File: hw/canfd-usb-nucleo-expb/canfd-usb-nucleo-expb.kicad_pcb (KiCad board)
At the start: 2 copper layers, 70 x 59 mm, 52 parts, among them CN10 CONN, CN7 POWER, J3 Conn_01x03, J4 Conn_01x03, J5 Conn_01x03, SW1 SW_Push_Dual_x2, SW2 SW_Push_Dual_x2, SW3 SW_Push_Dual_x2, U2 ATA6561-GAQW-N, U3 ATA6561-GAQW-N, U4 ATA6561-GAQW-N

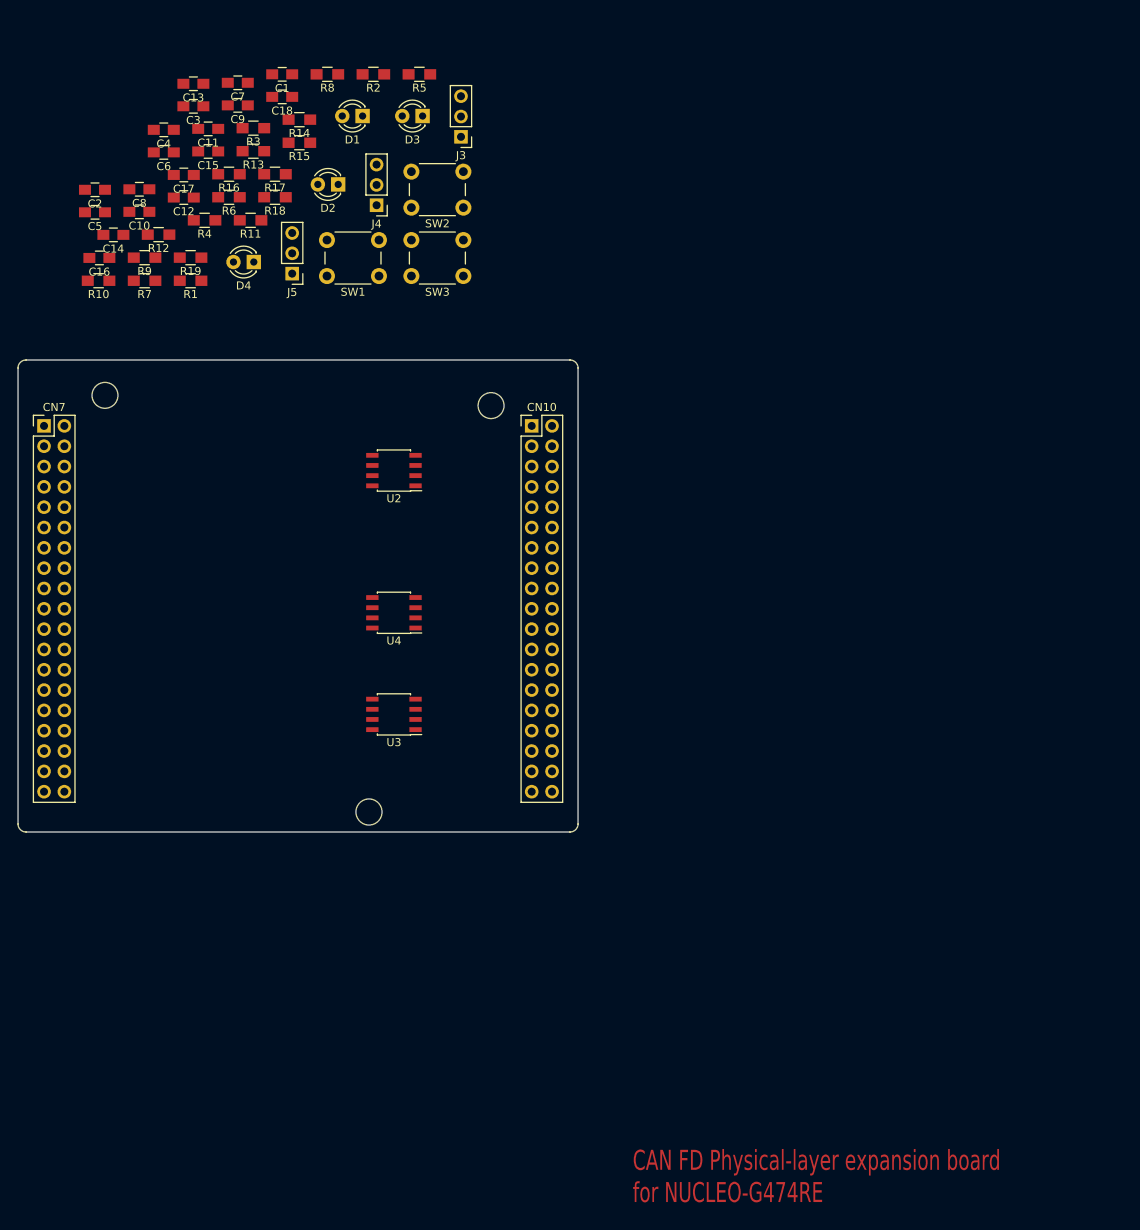
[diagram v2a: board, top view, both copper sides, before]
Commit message: HW: Added footprints for all components
Created the footprint for USB-Type-C connector
Added footprints for the rest of the components on the PCB.
Started the mock-up placement of components on the board

Signed-off-by: AlexeyZ <silkt207@gmail.com>
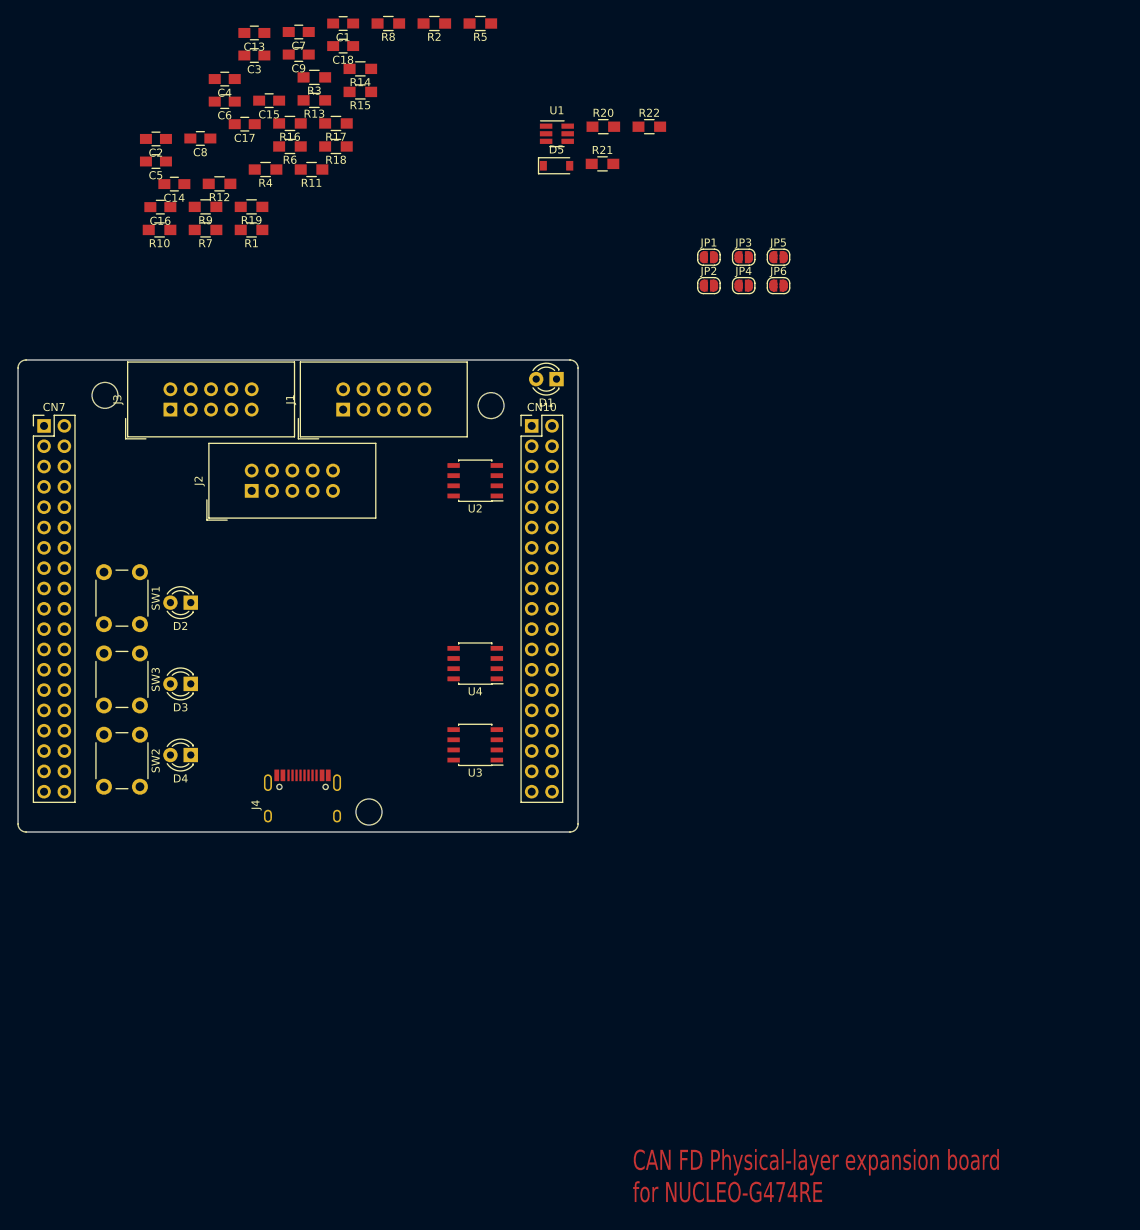
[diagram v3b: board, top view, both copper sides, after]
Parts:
- removed C10, C11, C12: 100p, Capacitors_SMD:C_0805_HandSoldering
- removed J5: Conn_01x03, Pin_Headers:Pin_Header_Straight_1x03_Pitch2.54mm
- added D5: D_Schottky, Diodes_SMD:D_SOD-123, F.Cu at (169.5, 45.6)
- added J1: Conn_01x10, can-usb:IDC-Header_2x05_P2.54mm_Vertical, F.Cu at (142.9, 76.1)
- added J2: Conn_01x10, can-usb:IDC-Header_2x05_P2.54mm_Vertical, F.Cu at (131.4, 86.2)
- added JP1: Jumper_2_Open, can-usb:SolderJumper-2_P1.3mm_Open_RoundedPad1.0x1.5mm, F.Cu at (188.6, 57.0)
- added JP2: Jumper_2_Open, can-usb:SolderJumper-2_P1.3mm_Open_RoundedPad1.0x1.5mm, F.Cu at (188.6, 60.6)
- added JP3: Jumper_2_Open, can-usb:SolderJumper-2_P1.3mm_Open_RoundedPad1.0x1.5mm, F.Cu at (192.9, 57.0)
- added JP4: Jumper_2_Open, can-usb:SolderJumper-2_P1.3mm_Open_RoundedPad1.0x1.5mm, F.Cu at (192.9, 60.6)
- added JP5: Jumper_2_Open, can-usb:SolderJumper-2_P1.3mm_Open_RoundedPad1.0x1.5mm, F.Cu at (197.3, 57.0)
- added JP6: Jumper_2_Open, can-usb:SolderJumper-2_P1.3mm_Open_RoundedPad1.0x1.5mm, F.Cu at (197.3, 60.6)
- added R20: 100R, Resistors_SMD:R_0805_HandSoldering, F.Cu at (175.4, 40.7)
- added R21: 100R, Resistors_SMD:R_0805_HandSoldering, F.Cu at (175.3, 45.4)
- added R22: 100R, Resistors_SMD:R_0805_HandSoldering, F.Cu at (181.1, 40.7)
- added U1: USBLC6-2SC6, TO_SOT_Packages_SMD:SOT-23-6_Handsoldering, F.Cu at (169.6, 41.6)
- C4: value 15p -> 10nf
- C5: value 15p -> 22u
- C6: value 15p -> 2.2u
- J3: value Conn_01x03 -> Conn_01x10; footprint Pin_Headers:Pin_Header_Straight_1x03_Pitch2.54mm -> can-usb:IDC-Header_2x05_P2.54mm_Vertical
- J4: value Conn_01x03 -> USB_C_Receptacle_USB2.0; footprint Pin_Headers:Pin_Header_Straight_1x03_Pitch2.54mm -> can-usb:L-KLS1-TIPEC-B
- R1: value 62R -> 220k
- R12: value 100k -> 5.1k
- R13, R14, R19: value 100k -> 10k
- R15, R16, R17, R18: value 100k -> 510R
- R2, R3, R4: value 62R -> 1k
- R5: value 62R -> 5.1k
- moved SW2 77.3 mm to (117.5, 116.7), turned to 270 degrees
- moved D3 76.7 mm to (123.8, 110.4)
- moved J4 71.9 mm to (137.8, 121.8), turned to 0 degrees
- moved SW3 62.1 mm to (117.5, 106.6), turned to 270 degrees
- moved D4 62.1 mm to (123.8, 119.3)
- moved D2 55.4 mm to (123.8, 100.2)
- moved J3 49.8 mm to (121.3, 76.1), turned to 90 degrees
- moved SW1 47.6 mm to (117.5, 96.4), turned to 270 degrees
- moved D1 40.9 mm to (169.5, 72.3)
- moved U4 12.0 mm to (159.4, 107.8)
- moved U3 10.9 mm to (159.4, 118.0)
- moved U2 10.2 mm to (159.4, 85.0)
- moved C13 9.92 mm to (131.8, 29.0)
- moved C16 9.92 mm to (120.0, 50.8)
- moved C8 9.92 mm to (125.0, 42.2)
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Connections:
- C16 pad 1: +3V3 -> Net-(C16-Pad1)
- C17 pad 1: +3V3 -> Net-(C17-Pad1)
- C18 pad 1: +3V3 -> Net-(C18-Pad1)
- C4 pad 1: RX1 -> Net-(C4-Pad1)
- C5 pad 1: RX2 -> +5V
- C6 pad 1: RX3 -> +3V3
- CN10 pad 22: (no net) -> Net-(CN10-Pad22)
- CN10 pad 24: (no net) -> Net-(CN10-Pad24)
- CN10 pad 26: (no net) -> Net-(CN10-Pad26)
- CN7 pad 20: (no net) -> GND
- CN7 pad 8: GND -> (no net)
- J3 pad 1: +3V3 -> (no net)
- J3 pad 2: STANDBY_1 -> CAN3_L
- R1 pad 1: Net-(J1-Pad3) -> GND
- R1 pad 2: D+ -> Net-(C4-Pad1)
- R12 pad 1: GND -> Net-(J4-PadA5)
- R12 pad 2: Net-(J1-Pad4) -> GND
- R2 pad 1: Net-(J1-Pad2) -> Net-(CN10-Pad22)
- R2 pad 2: D- -> STANDBY_1
- R3 pad 1: CAN1_H -> Net-(CN10-Pad24)
- R3 pad 2: CAN1_L -> STANDBY_2
- R4 pad 1: CAN2_H -> Net-(CN10-Pad26)
- R4 pad 2: CAN2_L -> STANDBY_3
- R5 pad 1: CAN3_H -> Net-(J4-PadB5)
- R5 pad 2: CAN3_L -> GND
- U2 pad 8: STANDBY_1 -> Net-(JP1-Pad2)
- U3 pad 8: STANDBY_2 -> Net-(JP2-Pad2)
- U4 pad 8: STANDBY_3 -> Net-(JP3-Pad2)

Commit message: HW: Footprints and components layout
Added footprints for all components and created a new one for USB
connector. Started the components layout with positioning of all
components on the PCB before laying out the traces.

Signed-off-by: AlexeyZ <silkt207@gmail.com>
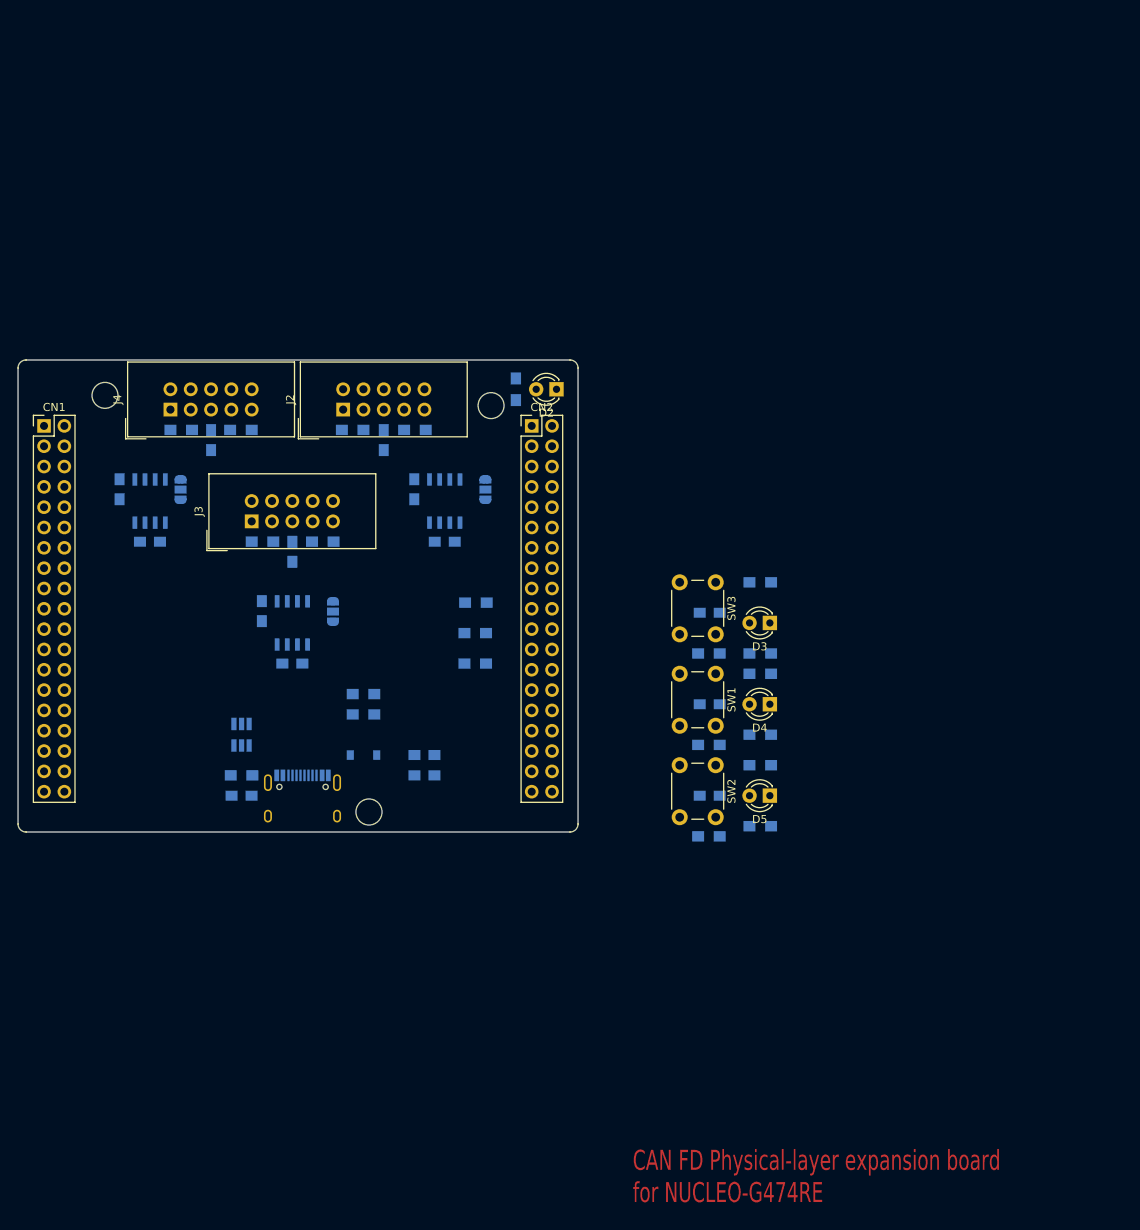
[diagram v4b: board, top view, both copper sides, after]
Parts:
- removed C16, C17, C18: 100n, Capacitors_SMD:C_0805_HandSoldering
- removed the C3 at (131.8, 31.8)
- removed the D2 at (123.8, 100.2)
- removed the J1 at (142.9, 76.1)
- removed JP4, JP5, JP6: Jumper_2_Open, can-usb:SolderJumper-2_P1.3mm_Open_RoundedPad1.0x1.5mm
- removed the R10 at (119.9, 53.6)
- removed the R19 at (131.4, 50.7)
- removed the R22 at (181.1, 40.7)
- removed the R6 at (136.2, 43.2)
- removed the R9 at (125.7, 50.7)
- added C4: 100n, Capacitors_SMD:C_0805_HandSoldering, B.Cu at (188.7, 112.9)
- added C5: 100n, Capacitors_SMD:C_0805_HandSoldering, B.Cu at (188.7, 124.3)
- added C6: 100n, Capacitors_SMD:C_0805_HandSoldering, B.Cu at (188.7, 101.5)
- added C8: 100n, Capacitors_SMD:C_0805_HandSoldering, B.Cu at (118.7, 92.6)
- added D1: D_Schottky, Diodes_SMD:D_SOD-123, B.Cu at (145.4, 119.3)
- added J2: Conn_01x10, can-usb:IDC-Header_2x05_P2.54mm_Vertical, F.Cu at (142.9, 76.1)
- added R11: 510R, Resistors_SMD:R_0805_HandSoldering, B.Cu at (195.0, 106.6)
- added R12: 510R, Resistors_SMD:R_0805_HandSoldering, B.Cu at (195.0, 116.7)
- added R14: 100R, Resistors_SMD:R_0805_HandSoldering, B.Cu at (195.0, 109.1)
- added R15: 10k, Resistors_SMD:R_0805_HandSoldering, B.Cu at (188.6, 106.6)
- added R8: 100R, Resistors_SMD:R_0805_HandSoldering, B.Cu at (195.0, 120.5)
- C1: renamed from C4; moved to B.Cu
- C10: renamed from C7; moved to B.Cu
- C11: renamed from C8; moved to B.Cu
- C12: renamed from C9; moved to B.Cu
- C13, C14, C15, R1, R2, R3, R4, R5, U1, U2, U3, U4: moved to B.Cu
- C2: renamed from C5; moved to B.Cu
- C3: renamed from C6; moved to B.Cu
- C7: renamed from C1; moved to B.Cu
- C9: renamed from C2; moved to B.Cu
- D3: value STATUS2 -> STATUS1
- D4: value STATUS3 -> STATUS2
- D5: value D_Schottky -> STATUS3; footprint Diodes_SMD:D_SOD-123 -> LEDs:LED_D3.0mm
- J1: renamed from J4; moved to B.Cu
- JP1, JP2, JP3: value Jumper_2_Open -> Jumper_3_Open; footprint can-usb:SolderJumper-2_P1.3mm_Open_RoundedPad1.0x1.5mm -> can-usb:SolderJumper-3_P1.3mm_Open_RoundedPad1.0x1.5mm; moved to B.Cu
- R10: renamed from R15; moved to B.Cu
- R13: value 10k -> 510R; moved to B.Cu
- R16: value 510R -> 100R; moved to B.Cu
- R17, R18: value 510R -> 62R; moved to B.Cu
- R19: renamed from R8; moved to B.Cu
- R20, R21: value 100R -> 62R; moved to B.Cu
- R22: renamed from R11; moved to B.Cu
- R6: renamed from R12; moved to B.Cu
- R7: value 62R -> 10k; moved to B.Cu
- R9: renamed from R14; moved to B.Cu
- SW1, SW2, SW3: footprint Buttons_Switches_THT:SW_PUSH_6mm -> Button_Switch_THT:SW_PUSH_6mm
- moved R13 106.5 mm to (195.0, 128.1)
- moved R9 105.4 mm to (188.6, 129.4)
- moved R7 90.0 mm to (188.6, 118.0)
- moved C1 89.6 mm to (130.2, 124.3)
- moved R5 87.6 mm to (145.4, 114.2), turned to 0 degrees
- moved C3 85.4 mm to (153.0, 119.3), turned to 0 degrees
- moved U1 84.8 mm to (130.2, 116.7), turned to 90 degrees
- moved C2 83.7 mm to (153.0, 121.8), turned to 0 degrees
- moved D5 83.1 mm to (196.2, 124.3), turned to 180 degrees
- moved R16 82.1 mm to (195.0, 97.7), turned to 0 degrees
- moved C7 80.3 mm to (136.5, 107.8), turned to 0 degrees
- moved JP3 76.1 mm to (122.6, 86.1), turned to 270 degrees
- moved SW1 73.1 mm to (189.4, 109.1)
- moved D3 72.8 mm to (196.2, 102.7)
- moved D4 72.7 mm to (196.2, 112.9)
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- renumbered CN7 to CN1, CN10 to CN2, D1 to D2, J2 to J3, J3 to J4
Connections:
- net CAN2_H renamed CAN2_H+
- net CAN3_L renamed CAN3_L-
- D5 pad 1: +5V -> GND
- J1 pad A4: Net-(D5-Pad2) -> Net-(D1-Pad2)
- J1 pad A8: Net-(J4-PadA8) -> (no net)
- J1 pad A9: Net-(D5-Pad2) -> Net-(D1-Pad2)
- J1 pad B8: Net-(J4-PadB8) -> (no net)
- J3 pad 2: CAN2_L -> CAN2_L+
- J4 pad 7: CAN3_H -> CAN3_H+
- R13 pad 1: SW1 -> LED4
- R13 pad 2: GND -> Net-(D5-Pad2)
- R16 pad 1: LED2 -> +3V3
- R17 pad 1: LED3 -> CAN1_H+
- R17 pad 2: Net-(D3-Pad2) -> Net-(C13-Pad1)
- R18 pad 1: LED4 -> Net-(C13-Pad1)
- R18 pad 2: Net-(D4-Pad2) -> CAN1_L-
- R20 pad 1: +3V3 -> Net-(C14-Pad1)
- R20 pad 2: Net-(C16-Pad1) -> CAN2_L+
- R21 pad 1: +3V3 -> CAN3_H+
- R21 pad 2: Net-(C17-Pad1) -> Net-(C15-Pad1)
- R7 pad 1: Net-(C13-Pad1) -> SW1
- R7 pad 2: CAN1_L -> GND
- SW1 pad 1: SW3 -> SW1
- SW3 pad 1: SW1 -> SW3
- U1 pad 3: Net-(U1-Pad3) -> (no net)
- U1 pad 4: Net-(U1-Pad4) -> (no net)
- U1 pad 5: Net-(D5-Pad2) -> Net-(D1-Pad2)
- U2 pad 6: CAN1_L -> CAN1_L-
- U2 pad 7: CAN1_H -> CAN1_H+
- U3 pad 6: CAN2_L -> CAN2_L+
- U4 pad 7: CAN3_H -> CAN3_H+
